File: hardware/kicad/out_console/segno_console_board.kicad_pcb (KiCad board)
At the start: 2 copper layers, 99.5 x 99.5 mm, 65 parts, among them J1 RaspberryPi_Pico_SMD_HandSold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, J10 JST_XH_B2B-XH-A_1x02_P2.50mm_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, J11 JST_XH_B2B-XH-A_1x02_P2.50mm_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, J12 JST_XH_B2B-XH-A_1x02_P2.50mm_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, J13 JST_XH_B2B-XH-A_1x02_P2.50mm_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, J14 JST_XH_B2B-XH-A_1x02_P2.50mm_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, J15 JST_XH_B2B-XH-A_1x02_P2.50mm_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, J16 JST_XH_B2B-XH-A_1x02_P2.50mm_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, J17 JST_XH_B2B-XH-A_1x02_P2.50mm_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, J18 JST_XH_B2B-XH-A_1x02_P2.50mm_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, J19 JST_XH_B2B-XH-A_1x02_P2.50mm_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, J2 IDC-Header_2x20_P2.54mm_Verti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, J20 JST_XH_B4B-XH-A_1x04_P2.50mm_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, J21 JST_XH_B4B-XH-A_1x04_P2.50mm_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, J22 PinHeader_2x03_P2.54mm_Vertic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, J23 JST_XH_B3B-XH-A_1x03_P2.50mm_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, J3 JST_XH_B4B-XH-A_1x04_P2.50mm_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, J4 JST_XH_B3B-XH-A_1x03_P2.50mm_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, J5 JST_XH_B2B-XH-A_1x02_P2.50mm_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, J6 JST_XH_B4B-XH-A_1x04_P2.50mm_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, J7 JST_XH_B3B-XH-A_1x03_P2.50mm_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, J8 JST_XH_B2B-XH-A_1x02_P2.50mm_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, J9 JST_XH_B2B-XH-A_1x02_P2.50mm_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, U1 DIP-14_W7.62mm, U2 DIP-6_W7.62mm

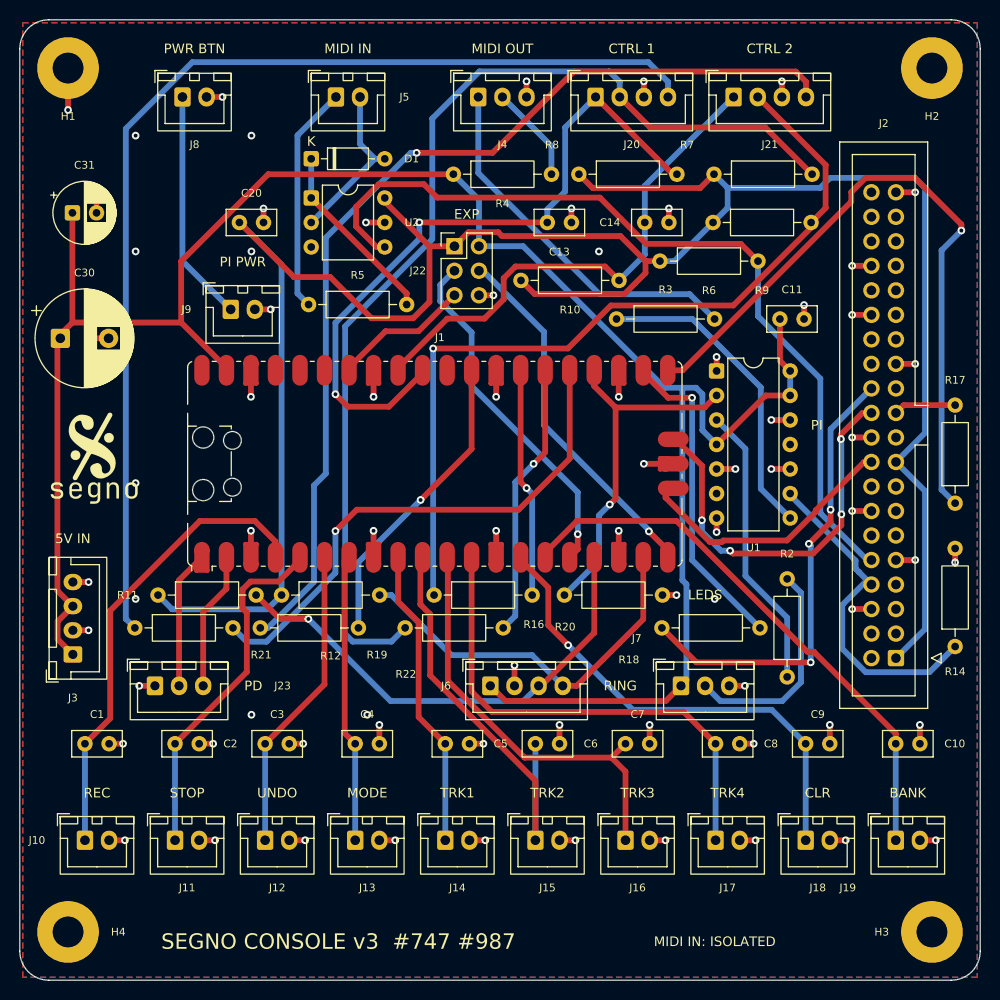
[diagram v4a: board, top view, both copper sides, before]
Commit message: refactor(hardware): the issue numbers come off the console silkscreen
The bottom strip printed "SEGNO CONSOLE v3  #747 #987". Issue numbers are
provenance for whoever edits the generator, not for whoever solders the
board: a tracker is not something you can look up with a board in your
hand, and the numbers age worse than the board does. The title is now just
"SEGNO CONSOLE v3". They stay in the file's docstring and in
console_board_mount.json, which is where that context is useful.

_silk() takes the text CENTRE, so dropping the numbers only shortens the
title inward and its clearance to H4's pad can only improve; the SILK gates
re-measure it as rendered either way and pass.

Re-placed and re-routed to regenerate it: clean on the second attempt, 0
violations and 0 unconnected, fab checks PASS, all 96 vias 0.8/0.4. The
back-silk wordmark ("segno console board v3") never carried numbers, and
the ring board's silk is just "SEGNO RING", so neither needed touching.
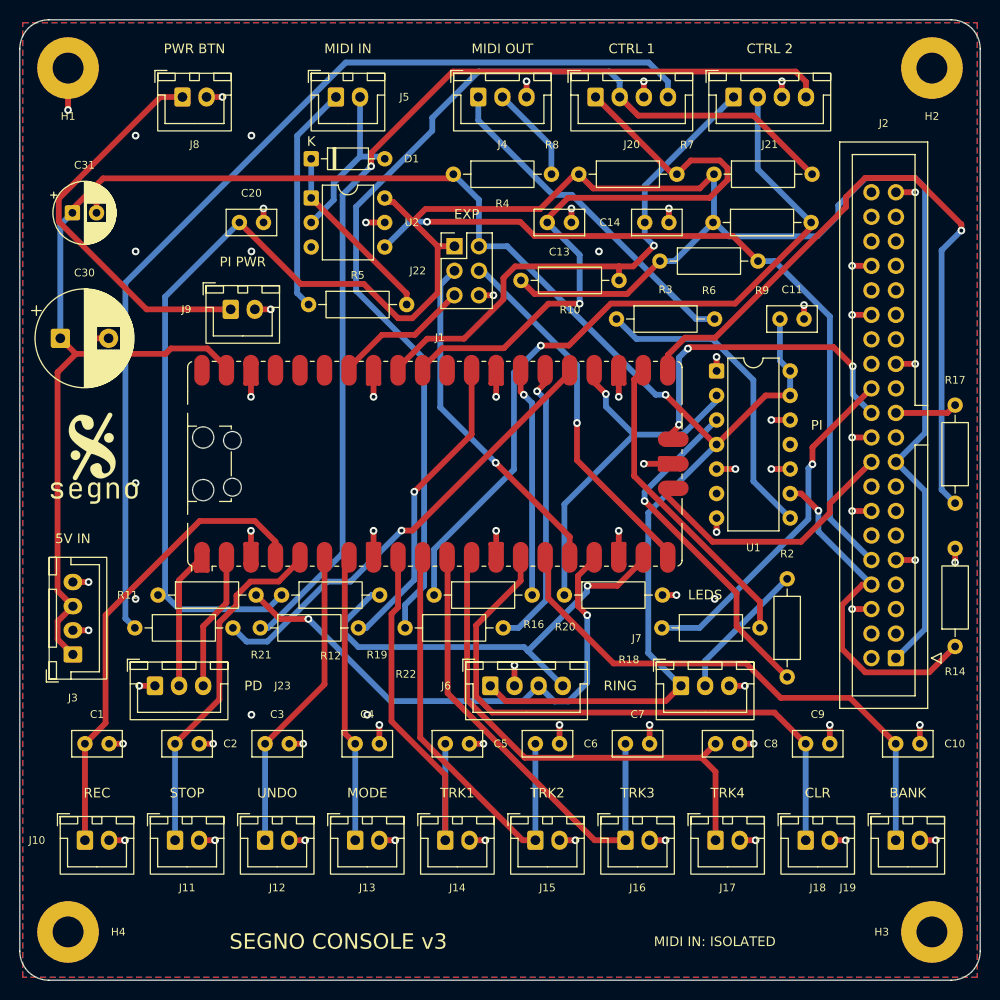
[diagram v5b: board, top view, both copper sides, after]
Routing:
- net PWR_BTN: track 24.1 -> 41.1 mm
- net SW_CLEAR: track 50.0 -> 62.5 mm, vias 1 -> 0
- net LINK_RX_PI: track 48.0 -> 36.1 mm, vias 3 -> 1
- net SW_TRACK1: track 31.3 -> 41.9 mm
- net MIDI_RX: track 87.9 -> 78.3 mm, vias 0 -> 1
- net J20_TN: track 113.5 -> 104.2 mm
- net IND_DATA_OUT: track 22.7 -> 14.6 mm
- net SWDIO: track 41.9 -> 34.0 mm, vias 4 -> 3
- net CTRL1_PRESENT: track 55.0 -> 47.3 mm
- net J21_REF: track 87.0 -> 79.3 mm
- net LINK_TO_CONSOLE: track 40.5 -> 47.2 mm, vias 0 -> 1
- net IND_DATA_BUF: track 29.6 -> 35.8 mm, vias 0 -> 1
- net LINK_TO_RING: track 50.3 -> 55.1 mm, vias 1 -> 2
- net SW_TRACK3: track 44.3 -> 48.8 mm
- net J20_REF: track 111.0 -> 106.5 mm
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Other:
- board text added: "SEGNO CONSOLE v3"
- board text removed: "SEGNO CONSOLE v3 #747 #987"
